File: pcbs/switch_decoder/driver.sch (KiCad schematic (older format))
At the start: 7 parts, among them Q1 2N7002, Q2 2N7002, U3 MIC4427

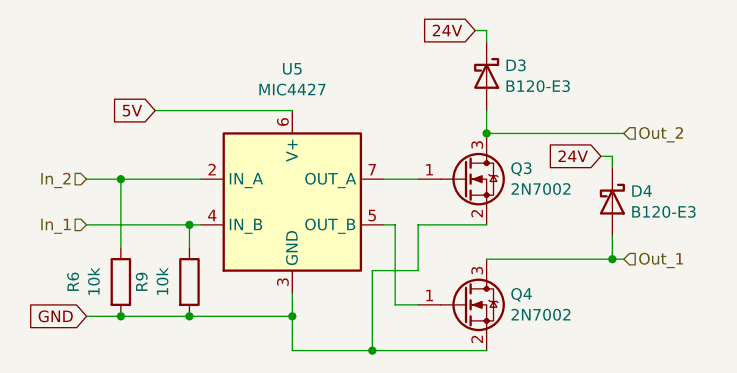
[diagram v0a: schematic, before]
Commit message: produced PCBs, dropped baudrate, removed on-board dynamic address selection - decoder must now be configured via programmer!
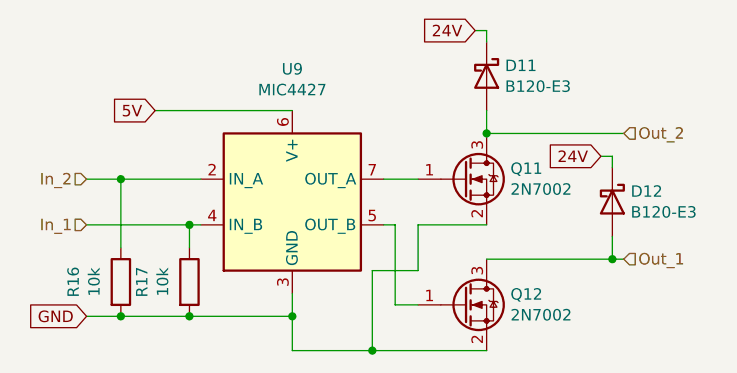
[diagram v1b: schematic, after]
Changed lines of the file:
@@
 AR Path="/60A3286C/60A8F884" Ref="U8"  Part="1"
 AR Path="/60A332A2/60A8F884" Ref="U9"  Part="1"
-F 0 "U5" H 5500 3981 50  0000 C CNN
+F 0 "U9" H 5500 3981 50  0000 C CNN
 F 1 "MIC4427" H 5500 3890 50  0000 C CNN
 F 2 "Package_SO:SOIC-8_3.9x4.9mm_P1.27mm" H 5500 3100 50  0001 C CNN
@@
 AR Path="/60A3286C/60A8F88A" Ref="R14"  Part="1"
 AR Path="/60A332A2/60A8F88A" Ref="R16"  Part="1"
-F 0 "R6" V 4543 3750 50  0000 C CNN
+F 0 "R16" V 4543 3750 50  0000 C CNN
 F 1 "10k" V 4634 3750 50  0000 C CNN
 F 2 "Resistor_SMD:R_0603_1608Metric" V 4680 3750 50  0001 C CNN
@@
 AR Path="/60A3286C/60A8F890" Ref="R15"  Part="1"
 AR Path="/60A332A2/60A8F890" Ref="R17"  Part="1"
-F 0 "R9" V 4843 3750 50  0000 C CNN
+F 0 "R17" V 4843 3750 50  0000 C CNN
 F 1 "10k" V 4934 3750 50  0000 C CNN
 F 2 "Resistor_SMD:R_0603_1608Metric" V 4980 3750 50  0001 C CNN
@@
 AR Path="/60A3286C/60A8F8A7" Ref="Q9"  Part="1"
 AR Path="/60A332A2/60A8F8A7" Ref="Q11"  Part="1"
-F 0 "Q3" H 6454 3346 50  0000 L CNN
+F 0 "Q11" H 6454 3346 50  0000 L CNN
 F 1 "2N7002" H 6454 3255 50  0000 L CNN
 F 2 "Package_TO_SOT_SMD:SOT-23" H 6450 3225 50  0001 L CIN
@@
 AR Path="/60A3286C/60A8F8AD" Ref="Q10"  Part="1"
 AR Path="/60A332A2/60A8F8AD" Ref="Q12"  Part="1"
-F 0 "Q4" H 6454 3896 50  0000 L CNN
+F 0 "Q12" H 6454 3896 50  0000 L CNN
 F 1 "2N7002" H 6454 3805 50  0000 L CNN
 F 2 "Package_TO_SOT_SMD:SOT-23" H 6450 3775 50  0001 L CIN
@@
 AR Path="/60A3286C/60A9334C" Ref="D9"  Part="1"
 AR Path="/60A332A2/60A9334C" Ref="D11"  Part="1"
-F 0 "D3" V 6304 2930 50  0000 L CNN
+F 0 "D11" V 6304 2930 50  0000 L CNN
 F 1 "B120-E3" V 6395 2930 50  0000 L CNN
 F 2 "Diode_SMD:D_SMA" H 6350 2675 50  0001 C CNN
@@
 AR Path="/60A3286C/60A953BC" Ref="D10"  Part="1"
 AR Path="/60A332A2/60A953BC" Ref="D12"  Part="1"
-F 0 "D4" V 6854 3480 50  0000 L CNN
+F 0 "D12" V 6854 3480 50  0000 L CNN
 F 1 "B120-E3" V 6945 3480 50  0000 L CNN
 F 2 "Diode_SMD:D_SMA" H 6900 3225 50  0001 C CNN
